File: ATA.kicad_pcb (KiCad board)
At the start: 2 copper layers, 20.3 x 36.8 mm, 12 parts, among them J1 TCOUPLE_IN, J2 Conn_01x08_Male, U1 AD8495, U2 AD8605

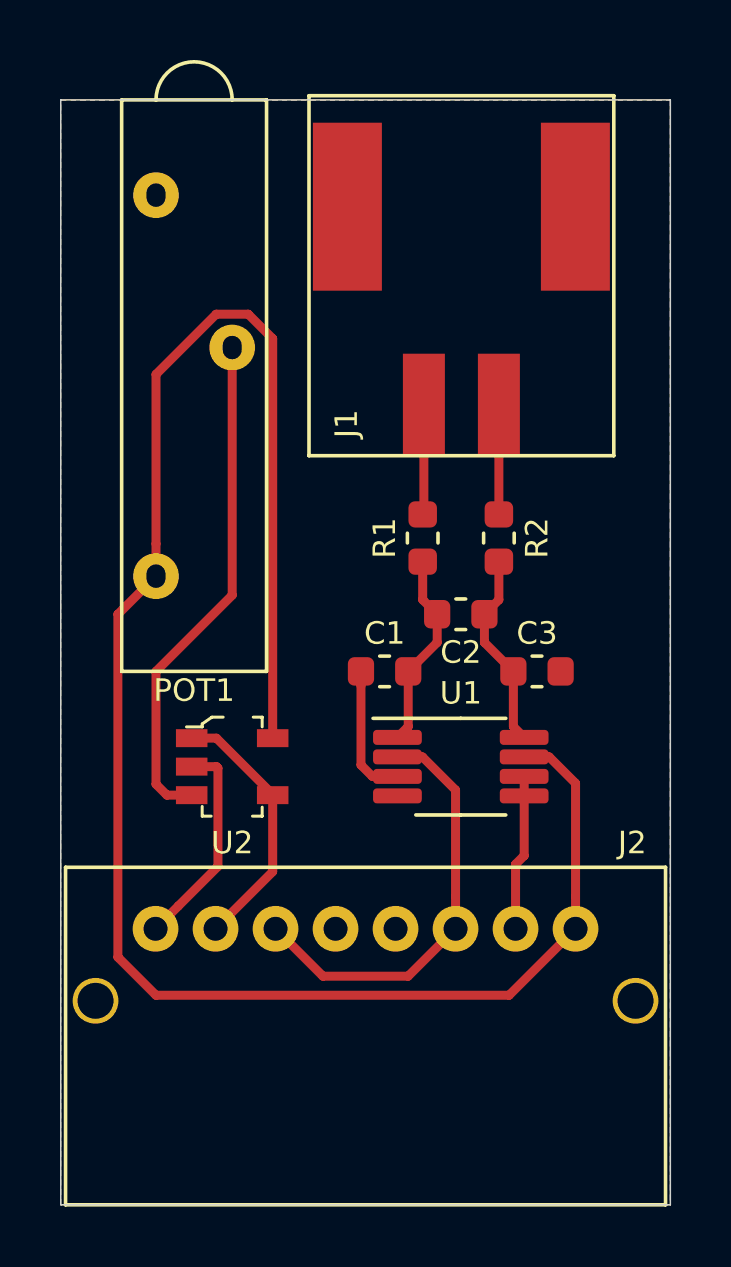
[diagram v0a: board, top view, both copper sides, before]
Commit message: Added voltage reference chip to high side of adjustable voltage divider reference
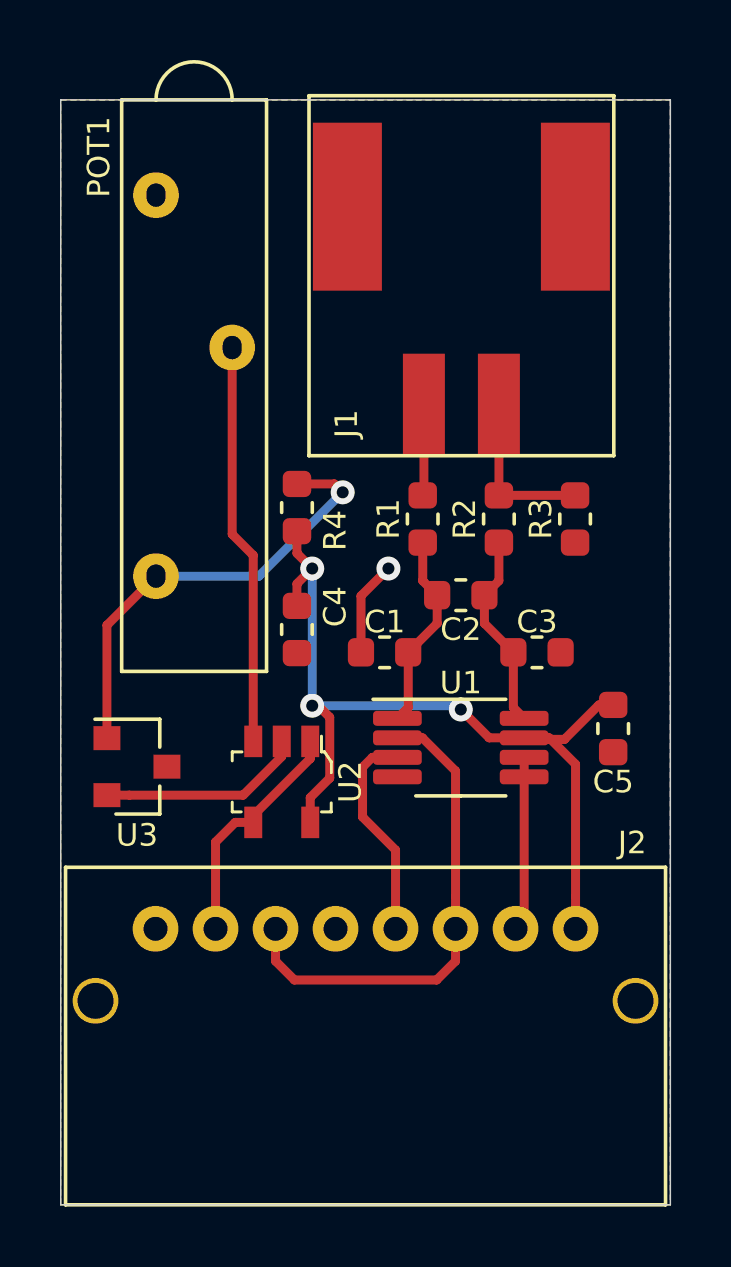
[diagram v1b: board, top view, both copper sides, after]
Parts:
- added C4: 0.1uF, Capacitor_SMD:C_0603_1608Metric, F.Cu at (143.8, 89.4)
- added C5: 0.1uF, Capacitor_SMD:C_0603_1608Metric, F.Cu at (154.3, 92.7)
- added R3: 1M, Resistor_SMD:R_0603_1608Metric, F.Cu at (153.0, 85.7)
- added R4: 1K, Resistor_SMD:R_0603_1608Metric, F.Cu at (143.8, 85.3)
- added U3: ADR5044BRTZ-REEL7, Package_TO_SOT_SMD:SOT-23, F.Cu at (138.4, 94.0)
- C1, C3: value C_Small -> 0.01uF
- C2: value C_Small -> 1uF
- R1, R2: value R_Small -> 100
- moved U2 1.73 mm to (143.3, 94.5), turned to 180 degrees
- moved C1 0.64 mm to (146.7, 90.2)
- moved C2 0.64 mm to (149.2, 88.3)
- moved C3 0.64 mm to (151.8, 90.2)
- moved R1 0.64 mm to (148.0, 85.7)
- moved R2 0.64 mm to (150.5, 85.7)
- moved U1 0.64 mm to (149.2, 93.3)
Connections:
- POT1 pad 1: VDD -> Net-(POT1-Pad1)
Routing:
- net VDD: track 62.0 -> 30.5 mm, vias 0 -> 3
- net Net-(POT1-Pad1): track 0.00 -> 15.1 mm, vias 0 -> 1
- net VSS: track 11.6 -> 17.4 mm, vias 0 -> 1
- net Net-(POT1-Pad2): track 16.9 -> 13.4 mm
- net VREF: track 14.3 -> 16.3 mm
- net Net-(J1-Pad1): track 3.66 -> 5.56 mm
- net Net-(J2-Pad2): track 8.75 -> 7.91 mm
- net Net-(J1-Pad2): track 3.67 -> 3.04 mm
- net Net-(J2-Pad7): track 5.20 -> 5.83 mm

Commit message: Rearranged placement a bit. Generated CAM files for v2
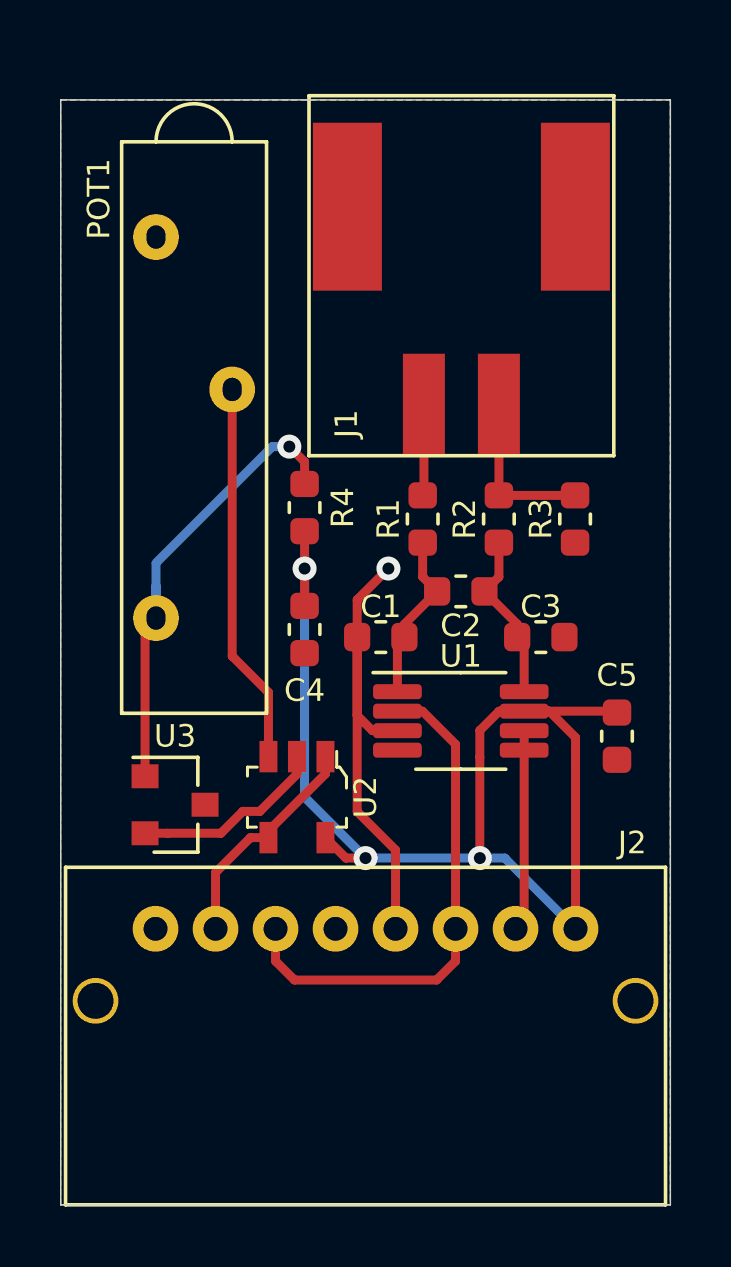
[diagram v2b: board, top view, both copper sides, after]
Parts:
- moved U3 1.80 mm to (139.7, 95.2)
- moved GRAPHIC2 1.53 mm to (146.8, 79.8)
- moved POT1 1.40 mm to (140.3, 73.2)
- moved U1 0.89 mm to (149.2, 92.5)
- moved U2 0.72 mm to (143.8, 95.0)
- moved C1 0.52 mm to (146.6, 89.7)
- moved C3 0.52 mm to (151.9, 89.7)
- moved C5 0.28 mm to (154.4, 93.0)
- moved C4 0.25 mm to (144.0, 89.4)
- moved GRAPHIC1 0.25 mm to (150.1, 92.1)
- moved R4 0.25 mm to (144.0, 85.3)
- moved C2 0.13 mm to (149.2, 88.1)
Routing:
- net VDD: track 30.5 -> 40.1 mm
- net VSS: track 17.4 -> 23.6 mm
- net Net-(C2-Pad2): track 6.61 -> 5.72 mm
- net Net-(C1-Pad1): track 6.61 -> 5.72 mm
- net VREF: track 16.3 -> 17.2 mm
- net Net-(J2-Pad7): track 5.83 -> 6.72 mm
- net Net-(POT1-Pad1): track 15.1 -> 15.8 mm
- net Net-(POT1-Pad2): track 13.4 -> 12.7 mm
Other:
- board text added: "V+ OUTPUT Z-REF V- N/C SELECT ADJUST V-"
- board text added: "V2.0"
- board text removed: "+5VDC OUTPUT Z-REF GROUND N/C SELECT ADJUST ZERO"
- board text removed: "V1.0"
